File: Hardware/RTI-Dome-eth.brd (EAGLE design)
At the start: 119.4 x 71.1 mm, 87 parts, among them IC1 24AA128ST, IC3 FT232RL, IC4 REG1117, IC5 74LVC245, IC6 74ABT245, J1 POWERPOLE_POWER45A, U1 W5500, X13 PN61729-S, X9 J1011F21PNL

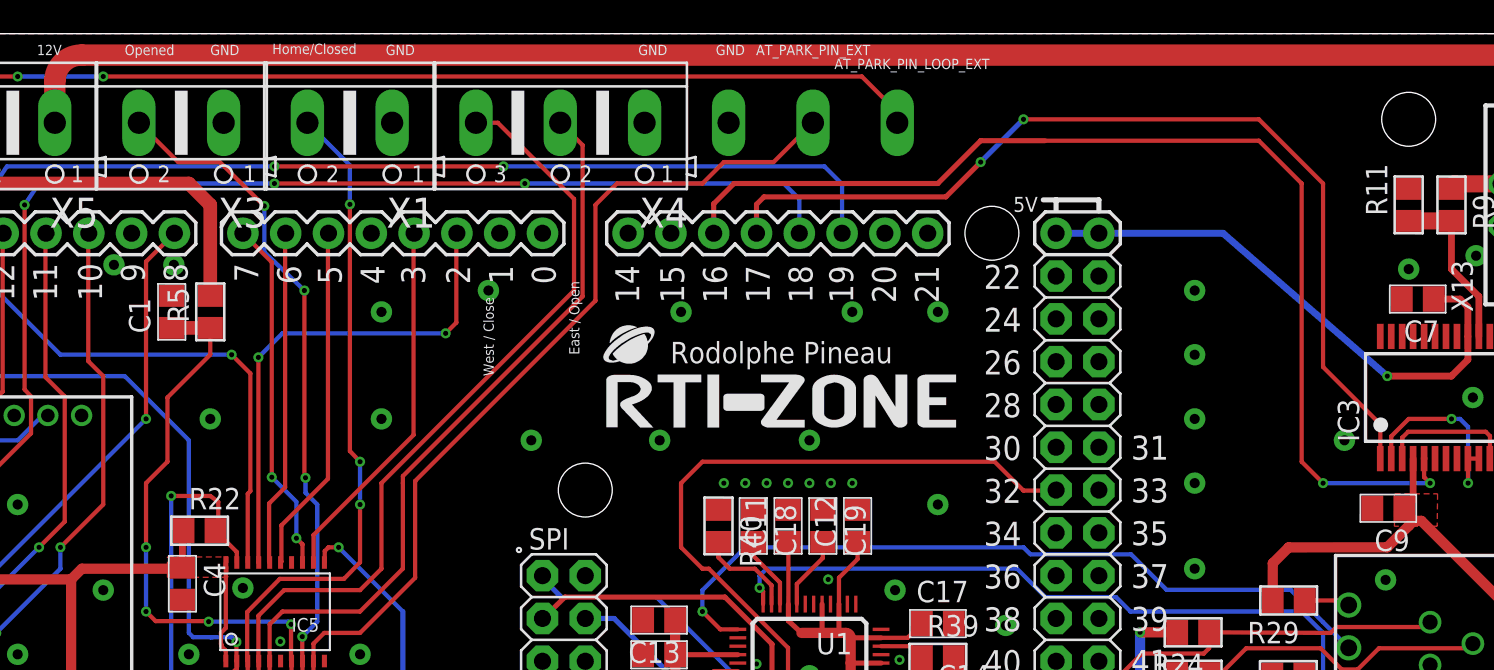
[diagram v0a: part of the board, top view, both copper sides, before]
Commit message: Fox termonal on eth board.
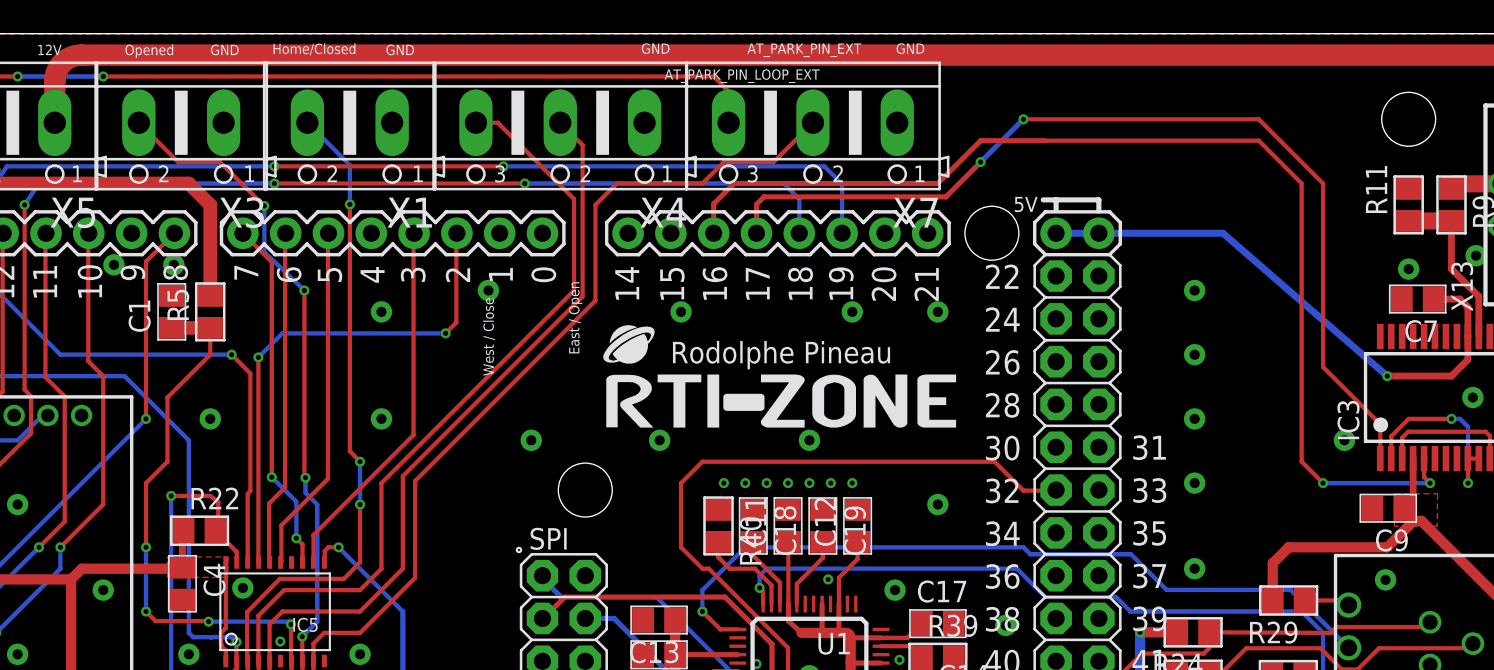
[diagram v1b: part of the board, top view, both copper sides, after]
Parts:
- flipped X7 to the top
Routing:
- net AT_PARK_PIN_LOOP_EXT: track 117.9 -> 108.6 mm
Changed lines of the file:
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@@
 <text x="49.8475" y="50.8" size="0.6096" layer="21" rot="R90">West / Close</text>
 <text x="57.15" y="69.88175" size="0.6096" layer="22" rot="MR0">East / Open</text>
-<text x="58.42" y="69.85" size="0.6096" layer="21">GND</text>
+<text x="58.59" y="69.93" size="0.6096" layer="21">GND</text>
 <text x="107.95" y="13.97" size="1.778" layer="21">GND</text>
 <text x="106.68" y="6.35" size="1.778" layer="21">+12V</text>
@@
 <text x="60.29325" y="68.54825" size="0.6096" layer="22" rot="MR0">GND</text>
 <text x="8.001" y="69.85" size="0.6096" layer="21">GND</text>
-<text x="63.021" y="69.85" size="0.6096" layer="21">GND</text>
-<text x="65.41" y="69.85" size="0.6096" layer="21">AT_PARK_PIN_EXT</text>
-<text x="70.059" y="69.0215" size="0.6096" layer="21">AT_PARK_PIN_LOOP_EXT</text>
+<text x="73.71" y="69.93" size="0.6096" layer="21">GND</text>
+<text x="64.89" y="69.93" size="0.6096" layer="21">AT_PARK_PIN_EXT</text>
+<text x="59.979" y="68.3915" size="0.6096" layer="21">AT_PARK_PIN_LOOP_EXT</text>
 <text x="78.355" y="69.85" size="0.6096" layer="22" rot="MR0">AT_PARK_PIN_LOOP_EXT</text>
 <text x="73.03" y="68.58" size="0.6096" layer="22" rot="MR0">AT_PARK_PIN_EXT</text>
@@
 <element name="R2" library="rti" package="R0805" value="100K 0.1%" x="41.49725" y="14.57325" rot="R90"/>
 <element name="C3" library="rti" package="C0805" value="10uF" x="34.9885" y="7.65175" rot="R270"/>
-<element name="X7" library="con-ptr500" package="AK500/3" value="" x="68.785" y="65.835" rot="MR180">
-<attribute name="MPN" value="" x="68.785" y="65.835" size="1.778" layer="28" rot="MR180" display="off"/>
-<attribute name="MF" value="" x="68.785" y="65.835" size="1.778" layer="28" rot="MR180" display="off"/>
-<attribute name="OC_NEWARK" value="unknown" x="68.785" y="65.835" size="1.778" layer="28" rot="MR180" display="off"/>
-<attribute name="OC_FARNELL" value="unknown" x="68.785" y="65.835" size="1.778" layer="28" rot="MR180" display="off"/>
+<element name="X7" library="con-ptr500" package="AK500/3" value="" x="68.785" y="65.835" rot="R180">
+<attribute name="MPN" value="" x="68.785" y="65.835" size="1.778" layer="27" rot="R180" display="off"/>
+<attribute name="MF" value="" x="68.785" y="65.835" size="1.778" layer="27" rot="R180" display="off"/>
+<attribute name="OC_NEWARK" value="unknown" x="68.785" y="65.835" size="1.778" layer="27" rot="R180" display="off"/>
+<attribute name="OC_FARNELL" value="unknown" x="68.785" y="65.835" size="1.778" layer="27" rot="R180" display="off"/>
 </element>
 <element name="X8" library="con-ptr500" package="AK500/2" value="" x="6.3" y="65.835" rot="R180">
@@
 <wire x1="6.35" y1="22.86" x2="6.35" y2="22.76725" width="0.3048" layer="1"/>
 <wire x1="6.35" y1="22.76725" x2="6.03" y2="22.44725" width="0.254" layer="1"/>
-<wire x1="71.69" y1="68.58" x2="26.67" y2="68.58" width="0.254" layer="1"/>
 <via x="26.67" y="68.58" extent="1-16" drill="0.3" diameter="0.254"/>
 <wire x1="26.67" y1="68.58" x2="21.59" y2="68.58" width="0.254" layer="16"/>
@@
 <wire x1="8.382" y1="25.019" x2="8.382" y2="24.892" width="0.254" layer="1"/>
 <wire x1="8.382" y1="24.892" x2="6.35" y2="22.86" width="0.254" layer="1"/>
-<wire x1="73.7888" y1="65.835" x2="73.7888" y2="66.4812" width="0.254" layer="1"/>
-<wire x1="73.7888" y1="66.4812" x2="71.69" y2="68.58" width="0.254" layer="1"/>
+<wire x1="26.67" y1="68.58" x2="62.901" y2="68.58" width="0.254" layer="1"/>
+<wire x1="62.901" y1="68.58" x2="63.7875" y2="67.6935" width="0.254" layer="1"/>
+<wire x1="63.7875" y1="67.6935" x2="63.7875" y2="65.8413" width="0.254" layer="1"/>
+<wire x1="63.7875" y1="65.8413" x2="63.7812" y2="65.835" width="0.254" layer="1"/>
 </signal>
 <signal name="AT_PARK_PIN_EXT">
@@
 <contactref element="R29" pad="2"/>
 <wire x1="96.07" y1="37.485" x2="96.075" y2="39.69" width="0.6096" layer="1"/>
-<wire x1="96.075" y1="39.69" x2="97.02" y2="40.635" width="0.6096" layer="1"/>
-<wire x1="97.02" y1="40.635" x2="102.87" y2="40.64" width="0.6096" layer="1"/>
+<wire x1="96.075" y1="39.69" x2="97.02" y2="40.64" width="0.6096" layer="1"/>
+<wire x1="97.02" y1="40.64" x2="102.87" y2="40.64" width="0.6096" layer="1"/>
 <wire x1="102.87" y1="40.64" x2="104.14" y2="41.91" width="0.6096" layer="1"/>
 <contactref element="U1" pad="28"/>

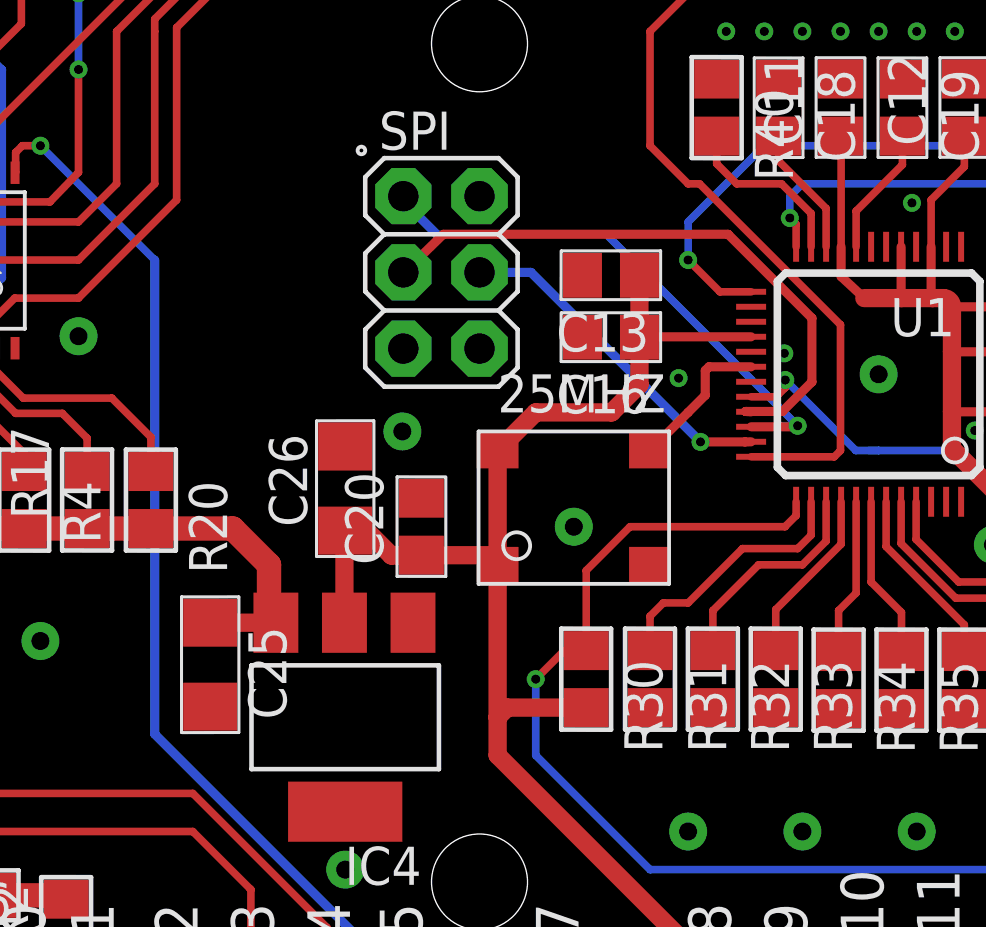
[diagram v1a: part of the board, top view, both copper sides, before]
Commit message: Fix ethernet LED.
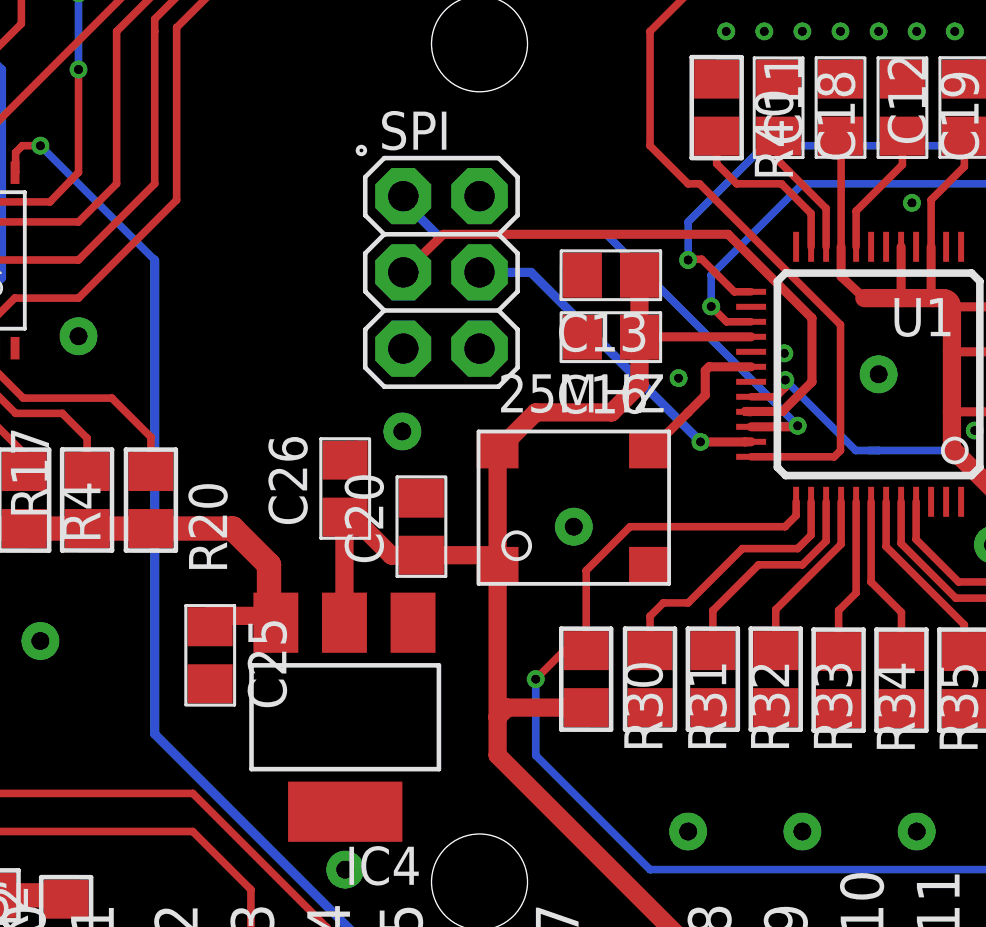
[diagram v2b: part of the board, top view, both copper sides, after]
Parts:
- C25, C26: device rti:C1206 -> rti:C0805
- moved C25 0.32 mm to (46.3, 23.7)
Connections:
- removed net N$18: U1.27
- removed net SPD_100: U1.24, X9.11
- new net ACT_LED: U1.27, X9.11
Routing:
- net ACT_LED: track 0.00 -> 48.9 mm, vias 0 -> 1
- net SPD_100: track 44.3 -> 0.00 mm, vias 1 -> 0
- net +3V3: track 146.1 -> 146.7 mm
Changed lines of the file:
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@@
 <attribute name="OC_FARNELL" value="1097566" x="50.8" y="21.59" size="1.778" layer="27" rot="R180" display="off"/>
 </element>
-<element name="C25" library="rti" package="C1206" value="10uF" x="46.3" y="23.34" rot="R270"/>
-<element name="C26" library="rti" package="C1206" value="10uF" x="50.8" y="29.21" rot="R90"/>
+<element name="C25" library="rti" package="C0805" value="10uF" x="46.3" y="23.655" rot="R270"/>
+<element name="C26" library="rti" package="C0805" value="10uF" x="50.8" y="29.21" rot="R90"/>
 <element name="C15" library="rti" package="C0805" value="6.8nF" x="96.995" y="28.88"/>
 <element name="C21" library="rti" package="C0805" value="6.8nF" x="96.995" y="26.8"/>
@@
 <wire x1="48.26" y1="26.67" x2="48.26" y2="24.9682" width="0.8128" layer="1"/>
 <wire x1="48.26" y1="24.9682" x2="48.4886" y2="24.7396" width="0.6096" layer="1"/>
-<wire x1="46.3" y1="24.74" x2="48.4882" y2="24.74" width="0.6096" layer="1"/>
-<wire x1="48.4882" y1="24.74" x2="48.4886" y2="24.7396" width="0.6096" layer="1"/>
+<wire x1="48.26" y1="24.9682" x2="46.3" y2="24.9682" width="0.6096" layer="1"/>
+<wire x1="46.3" y1="24.9682" x2="46.3" y2="24.605" width="0.6096" layer="1"/>
 <wire x1="48.26" y1="26.67" x2="83.21675" y2="59.27725" width="0" layer="19" extent="1-1"/>
 </signal>
@@
 <wire x1="65.4685" y1="32.5755" x2="65.4685" y2="32.8295" width="0.254" layer="1"/>
 </signal>
-<signal name="SPD_100">
-<contactref element="X9" pad="11"/>
-<contactref element="U1" pad="24"/>
-<via x="65.62" y="38.23" extent="1-16" drill="0.3"/>
-<wire x1="80.899" y1="39.37" x2="82.58175" y2="37.68725" width="0.254" layer="16"/>
-<wire x1="82.58175" y1="37.68725" x2="86.77275" y2="37.68725" width="0.254" layer="16"/>
-<wire x1="86.77275" y1="37.68725" x2="87.63" y2="36.83" width="0.254" layer="16"/>
-<wire x1="87.63" y1="36.83" x2="97.79" y2="36.83" width="0.254" layer="16"/>
-<wire x1="97.79" y1="36.83" x2="99.06" y2="35.56" width="0.254" layer="16"/>
-<wire x1="99.06" y1="35.56" x2="99.06" y2="30.345" width="0.254" layer="16"/>
-<wire x1="99.06" y1="30.345" x2="100.58" y2="28.825" width="0.254" layer="16"/>
-<wire x1="66.04" y1="39.37" x2="80.899" y2="39.37" width="0.254" layer="16"/>
-<wire x1="65.83" y1="37.27" x2="65.83" y2="38.02" width="0.254" layer="1"/>
-<wire x1="65.83" y1="38.02" x2="65.62" y2="38.23" width="0.254" layer="1"/>
-<wire x1="66.04" y1="39.37" x2="65.62" y2="38.95" width="0.254" layer="16"/>
-<wire x1="65.62" y1="38.95" x2="65.62" y2="38.23" width="0.254" layer="16"/>
-</signal>
 <signal name="LINK_ACK">
 <contactref element="X9" pad="10"/>
 <contactref element="U1" pad="25"/>
-<wire x1="64.33" y1="35.77" x2="63.29" y2="35.77" width="0.254" layer="1"/>
-<wire x1="63.29" y1="35.77" x2="62.23" y2="36.83" width="0.254" layer="1"/>
 <via x="62.23" y="36.83" extent="1-16" drill="0.3"/>
 <wire x1="62.23" y1="36.83" x2="62.23" y2="38.1" width="0.254" layer="16"/>
@@
 <wire x1="89.775" y1="38.115" x2="97.14" y2="38.115" width="0.254" layer="16"/>
 <wire x1="97.14" y1="38.115" x2="99.06" y2="36.195" width="0.254" layer="16"/>
+<wire x1="64.33" y1="35.77" x2="63.77" y2="35.77" width="0.254" layer="1"/>
+<wire x1="63.77" y1="35.77" x2="62.685" y2="36.855" width="0.254" layer="1"/>
+<wire x1="62.685" y1="36.855" x2="62.255" y2="36.855" width="0.254" layer="1"/>
+<wire x1="62.255" y1="36.855" x2="62.23" y2="36.83" width="0.254" layer="1"/>
 </signal>
 <signal name="N$7" class="3">
@@
 <contactref element="U1" pad="26"/>
 </signal>
-<signal name="N$18">
+<signal name="ACT_LED">
 <contactref element="U1" pad="27"/>
+<contactref element="X9" pad="11"/>
+<wire x1="80.899" y1="39.37" x2="82.58175" y2="37.68725" width="0.254" layer="16"/>
+<wire x1="82.58175" y1="37.68725" x2="86.77275" y2="37.68725" width="0.254" layer="16"/>
+<wire x1="86.77275" y1="37.68725" x2="87.63" y2="36.83" width="0.254" layer="16"/>
+<wire x1="87.63" y1="36.83" x2="97.79" y2="36.83" width="0.254" layer="16"/>
+<wire x1="97.79" y1="36.83" x2="99.06" y2="35.56" width="0.254" layer="16"/>
+<wire x1="99.06" y1="35.56" x2="99.06" y2="30.345" width="0.254" layer="16"/>
+<wire x1="99.06" y1="30.345" x2="100.58" y2="28.825" width="0.254" layer="16"/>
+<wire x1="66.04" y1="39.37" x2="80.899" y2="39.37" width="0.254" layer="16"/>
+<wire x1="66.04" y1="39.37" x2="63" y2="36.33" width="0.254" layer="16"/>
+<wire x1="63" y1="36.33" x2="63" y2="35.28" width="0.254" layer="16"/>
+<via x="63" y="35.28" extent="1-16" drill="0.3"/>
+<wire x1="63" y1="35.28" x2="63.51" y2="34.77" width="0.254" layer="1"/>
+<wire x1="63.51" y1="34.77" x2="64.33" y2="34.77" width="0.254" layer="1"/>
 </signal>
 <signal name="XI">
@@
 <wire x1="104.405" y1="43.445" x2="104.14" y2="43.18" width="0.4064" layer="1"/>
 <wire x1="50.7746" y1="24.7396" x2="50.7746" y2="27.7846" width="0.6096" layer="1"/>
-<wire x1="50.7746" y1="27.7846" x2="50.8" y2="27.81" width="0.6096" layer="1"/>
+<wire x1="50.7746" y1="27.7846" x2="50.8" y2="28.26" width="0.6096" layer="1"/>
 <contactref element="C9" pad="1"/>
 <polygon width="0.4064" layer="1" thermals="no">
@@
 <wire x1="64.33" y1="34.27" x2="60.62" y2="34.27" width="0.3048" layer="1"/>
 <wire x1="60.62" y1="34.27" x2="60.60825" y2="34.25825" width="0.3048" layer="1"/>
-<wire x1="50.8" y1="27.81" x2="51.51" y2="27.81" width="0.6096" layer="1"/>
+<wire x1="50.8" y1="28.26" x2="51.51" y2="27.81" width="0.6096" layer="1"/>
 <wire x1="51.51" y1="27.81" x2="52.34" y2="26.98" width="0.6096" layer="1"/>
 <wire x1="52.34" y1="26.98" x2="53.33" y2="26.98" width="0.6096" layer="1"/>
